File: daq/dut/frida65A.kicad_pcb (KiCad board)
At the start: 2 copper layers, 100 x 100 mm, 63 parts, among them J1 TP_PWR, J10 TP_LOGIC, J11 TP_OUT, J12 J_P, J13 469914004, J14 469914004, J15 469914004, J16 J_N, J2 CONN_IN_P, J3 CONN_IN_N, J4 TP_CFG, J5 CONN_CFG, J6 TP_IN, J7 TP_INIT, J8 TP_SAMP, J9 TP_COMP, U1 DUT, U2 THS4520RGTT

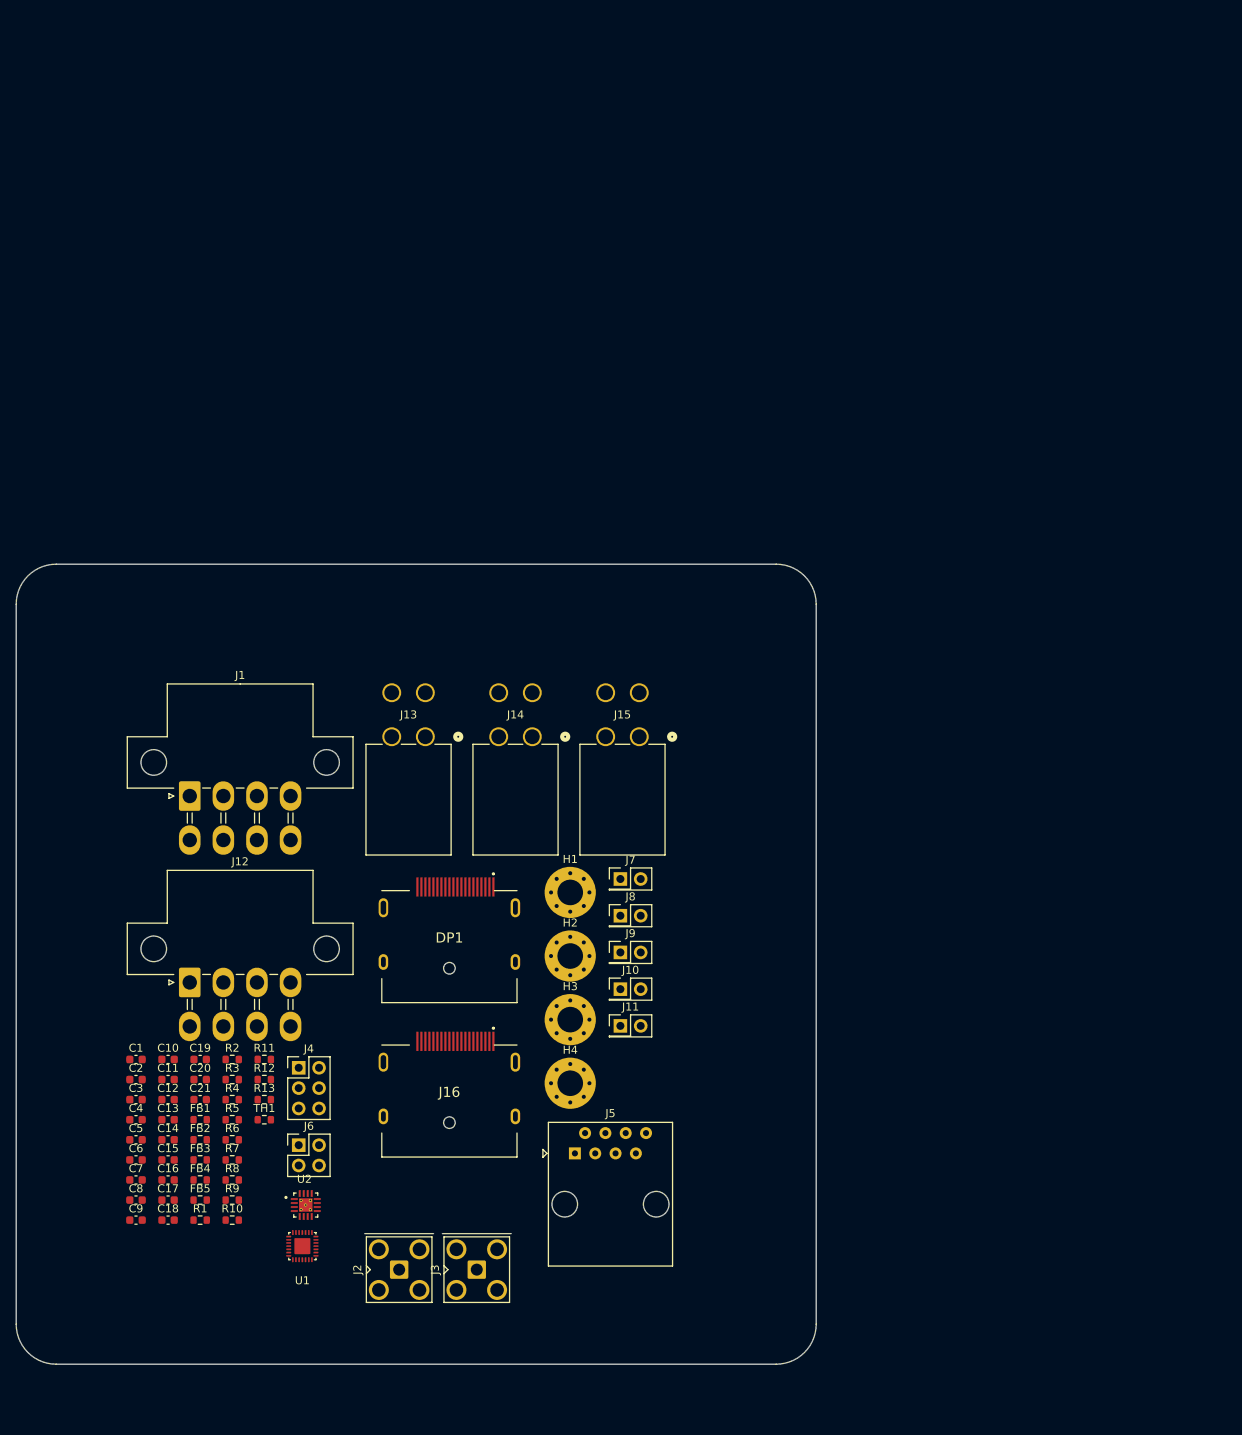
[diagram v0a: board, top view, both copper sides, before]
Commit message: Update PCB symbols, footprints, and models. Start work on Spectre simulator montecarlo support.
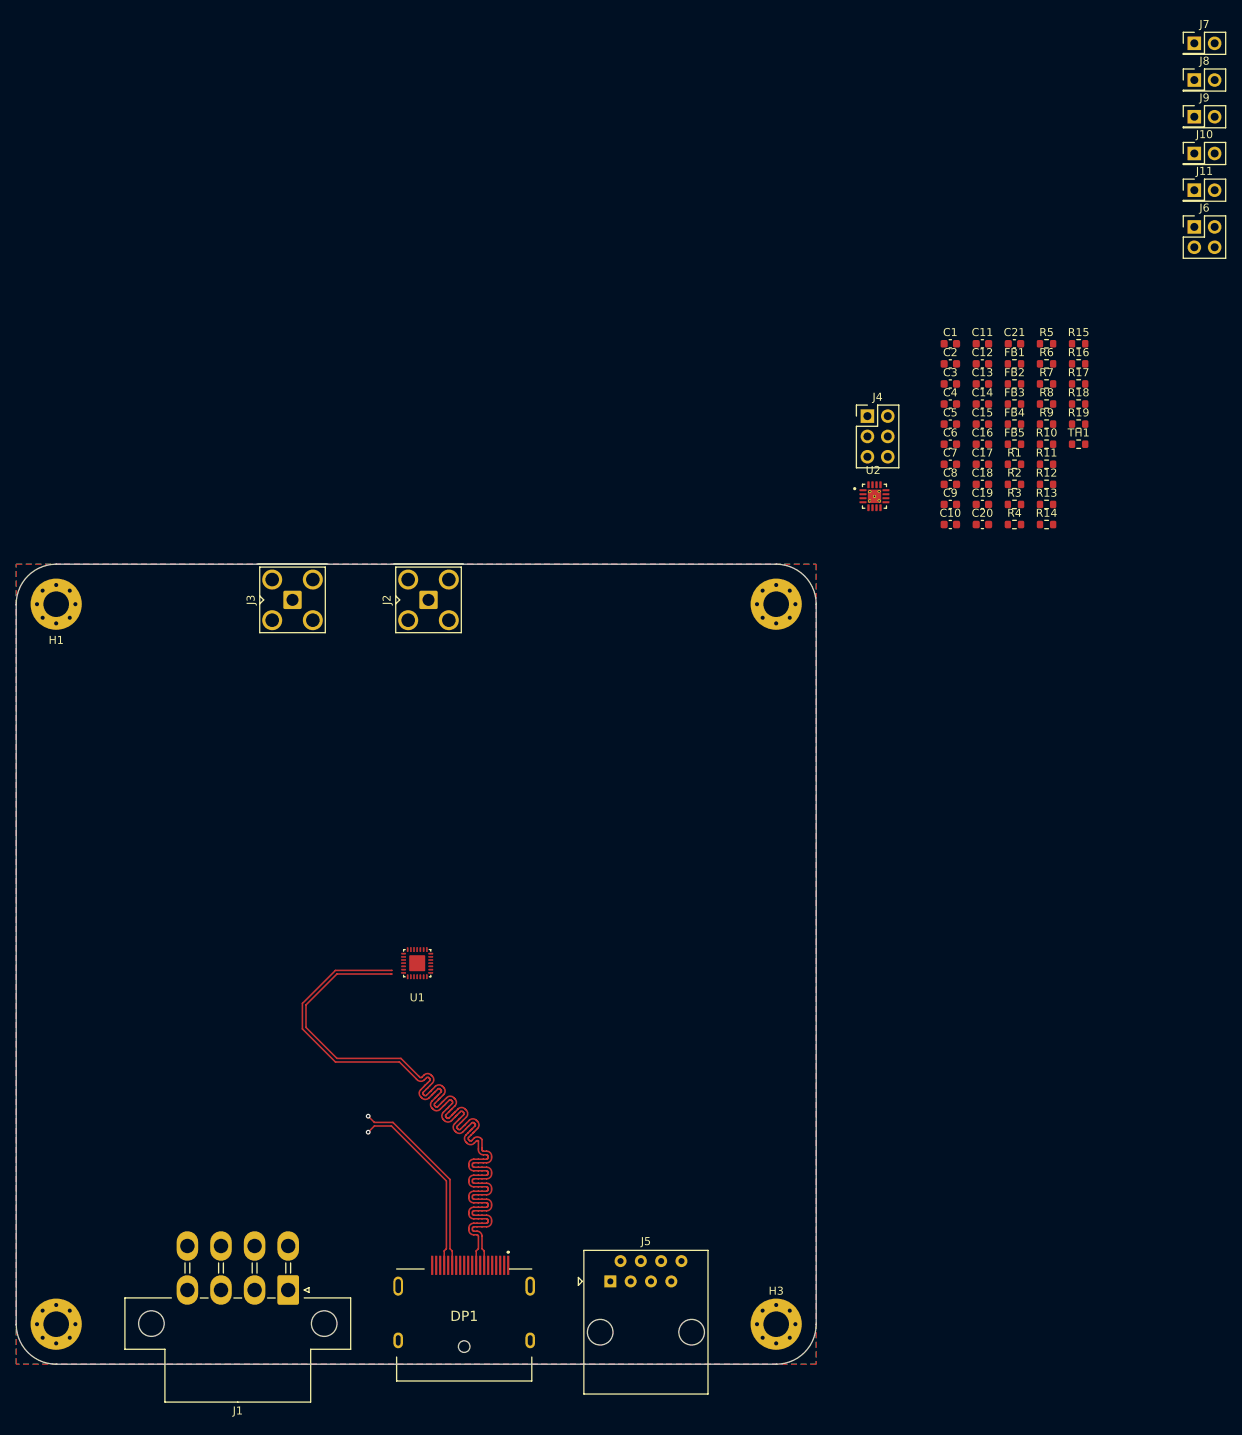
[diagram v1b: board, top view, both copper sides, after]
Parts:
- removed J12: J_P, frida65A:Molex_Mini-Fit_Jr_5569-08A1_2x04_P4.20mm_Horizontal
- removed J13, J14, J15: 469914004, frida65A:CONN_SD-46991-001_04_MOL
- removed J16: J_N, frida65A:displayport
- added R14: 499, Resistor_SMD:R_0603_1608Metric, F.Cu at (228.8, 45.0)
- added R15: 499, Resistor_SMD:R_0603_1608Metric, F.Cu at (232.8, 22.4)
- added R16: 499, Resistor_SMD:R_0603_1608Metric, F.Cu at (232.8, 25.0)
- added R17: 499, Resistor_SMD:R_0603_1608Metric, F.Cu at (232.8, 27.5)
- added R18: 1k, Resistor_SMD:R_0603_1608Metric, F.Cu at (232.8, 30.0)
- added R19: 1k, Resistor_SMD:R_0603_1608Metric, F.Cu at (232.8, 32.5)
- DP1: footprint frida65A:displayport -> frida:Molex_DisplayPort_472720024
- J1: footprint frida65A:Molex_Mini-Fit_Jr_5569-08A1_2x04_P4.20mm_Horizontal -> frida:Molex_MiniFitJr_469990014
- U1: footprint frida65A:frida -> frida:FRIDA_ASIC_Pad
- U2: footprint frida65A:QFN50P300X300X100-17N -> frida:QFN50P300X300X100-17N
- moved J6 160.3 mm to (247.3, 7.84)
- moved R10 140.6 mm to (228.8, 35.0)
- moved R5 140.6 mm to (228.8, 22.4)
- moved R6 140.6 mm to (228.8, 25.0)
- moved R7 140.6 mm to (228.8, 27.5)
- moved R8 140.6 mm to (228.8, 30.0)
- moved R9 140.6 mm to (228.8, 32.5)
- moved C21 138.9 mm to (224.8, 22.4)
- moved FB2 138.9 mm to (224.8, 27.5)
- moved R1 138.9 mm to (224.8, 37.5)
- moved FB1 138.9 mm to (224.8, 25.0)
- moved FB3 138.9 mm to (224.8, 30.0)
- moved FB4 138.9 mm to (224.8, 32.5)
- moved FB5 138.9 mm to (224.8, 35.0)
- moved C11 137.2 mm to (220.8, 22.4)
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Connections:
- J5 pad 6: unconnected-(J5-Pad6) -> /AMP_EN
- J6 pad 1: Net-(J12-Pin_3) -> Net-(J16-Pin_3)
- U2 pad 11: unconnected-(U2-VIN+-Pad11) -> Net-(U2-VIN+)
- U2 pad 12: unconnected-(U2-~{PD}-Pad12) -> Net-(U2-~{PD})
- U2 pad 2: unconnected-(U2-VIN--Pad2) -> Net-(U2-VIN-)
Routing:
- net /CLK_SAMP_P: track 0.00 -> 99.3 mm
- net /CLK_SAMP_N: track 0.00 -> 98.5 mm
- net /COMP_OUT_P: track 0.00 -> 45.3 mm, vias 0 -> 1
- net /COMP_OUT_N: track 0.00 -> 44.9 mm, vias 0 -> 1
- added copper zone on B.Cu, net GND
- added copper zone on F.Cu, net GND
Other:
- copper layers 2 -> 4
